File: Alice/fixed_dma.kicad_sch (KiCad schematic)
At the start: 146 parts, among them Q285 NOT_OC, Q286 NOT_OC, Q287 NOT_OC, Q288 NOT_OC, Q289 NOT_OC, Q290 NOT_OC, Q291 NOT_OC, Q292 NOT_OC, Q293 NOT_OC, Q294 NOT_OC, Q295 NOT_OC, Q296 NOT_OC, Q297 NOT_OC, Q298 NOT_OC, Q299 NOT_OC, Q300 NOT_OC, Q301 NOT_OC, Q302 NOT_OC, Q303 NOT_OC, Q304 NOT_OC, Q305 NOT_OC, Q306 NOT_OC, Q307 NOT_OC, Q308 NOT_OC, Q309 NOT_OC, Q310 NOT_OC, Q311 NOT_OC, Q312 NOT_OC, Q313 NOT_OC, Q314 NOT_OC, Q315 NOT_OC, Q316 NOT_OC, Q317 NOT_OC, Q318 NOT_OC, Q319 NOT_OC, Q320 NOT_OC, Q321 NOT_OC, Q322 NOT_OC, Q323 NOT_OC, Q324 NOT_OC, Q325 NOT_OC, Q326 NOT_OC, Q327 NOT_OC, Q328 NOT_OC, Q329 NOT_OC, Q330 NOT_OC, Q331 NOT_OC, Q332 NOT_OC

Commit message: Plane DMA sheet added
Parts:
- added NOR_23, NOR_25: NOR3, symbol NMOS:NOR3
- added NOR_24, NOR_26, NOR_27: NOR2, symbol NMOS:NOR2
- added RRW_FF1, RRW_FF2: DFF, symbol NMOS:DFF
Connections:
- net CCKF: now also RRW_FF2.4 (C1)
- net CCKQF: now also RRW_FF2.5 (C2)
- net DDBR: now also NOR_25.3
- net DKR: now also NOR_23.2
- net PHI1: now also RRW_FF1.4 (C1)
- net PHI2: now also RRW_FF1.5 (C2)
- net VCC: now also NOR_26.3
- new net: NOR_25.1, NOR_27.2
- new net: NOR_25.2, RRW_FF2.1 (Q)
- new net: NOR_24.1, NOR_25.4
- new net: NOR_26.1, NOR_27.3
- new net: RRW_FF1.1 (Q), RRW_FF2.3 (D)
- new net: NOR_23.1, RRW_FF1.3 (D)
- new net C1: NOR_24.2
- new net C3: NOR_24.3
- new net PAD_PRW: NOR_26.2
- new net PAD_RRW: NOR_27.1
- new net UBPD: NOR_23.4
- new net UBQD: NOR_23.3
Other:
- note added: "RE#"
- note added: "Refresh"
- moved on the sheet: RFP_FF1, URP_FF1

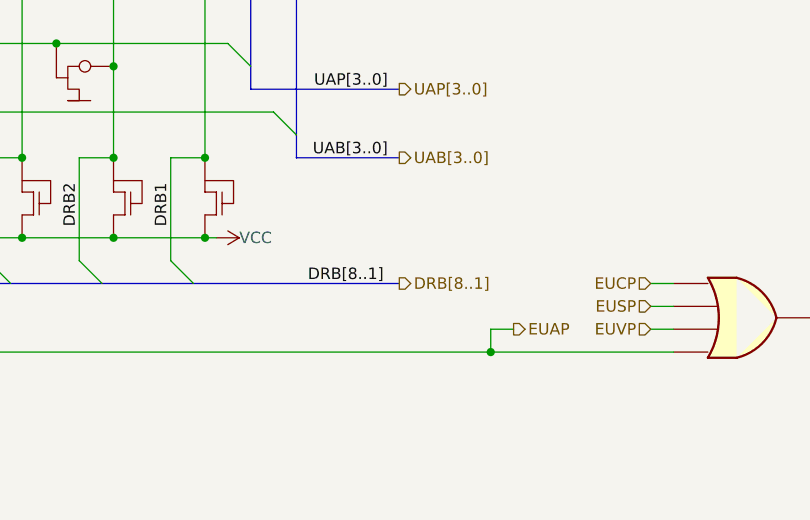
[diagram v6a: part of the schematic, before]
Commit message: Bitplane DMA runs in simulation
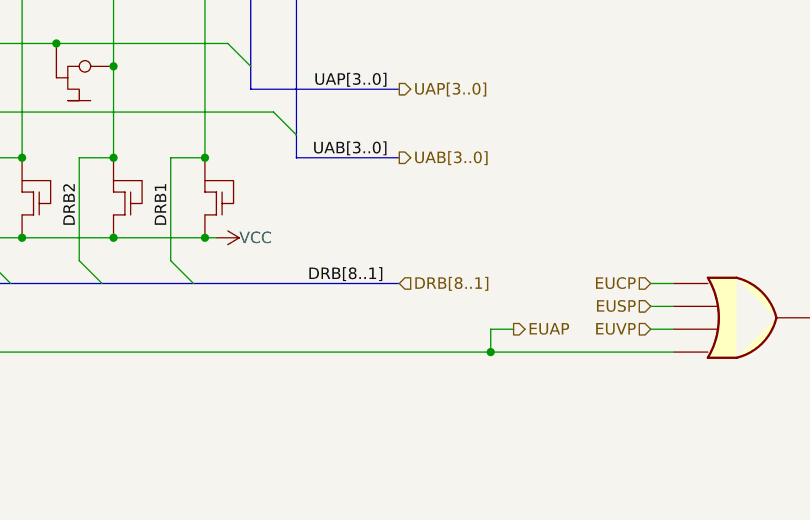
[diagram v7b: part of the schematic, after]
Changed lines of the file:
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@@
     (effects (font (size 1.27 1.27)) (justify left))
   )
-  (hierarchical_label "DRB[8..1]" (shape output) (at 256.54 332.74 0)
+  (hierarchical_label "DRB[8..1]" (shape input) (at 256.54 332.74 0)
     (effects (font (size 1.27 1.27)) (justify left))
   )

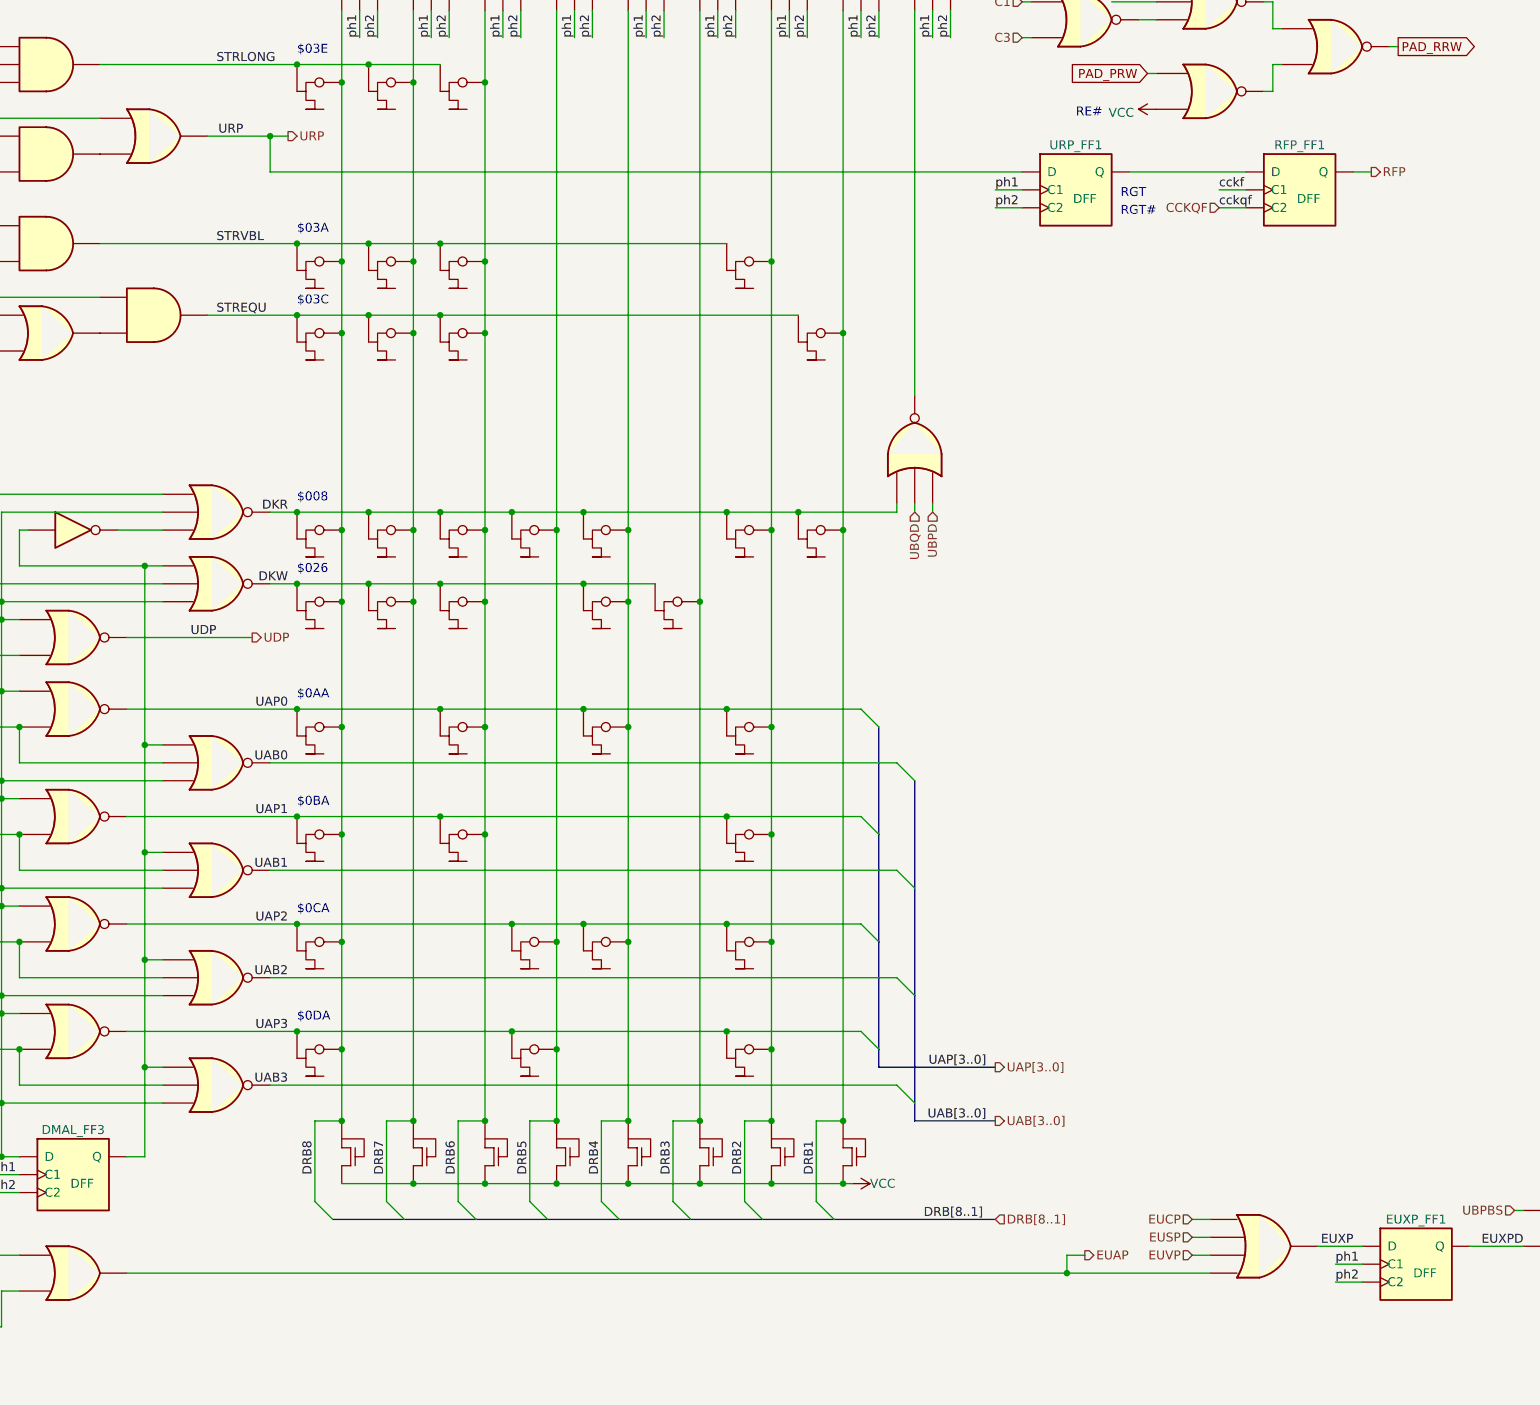
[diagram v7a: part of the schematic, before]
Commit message: Schematics have been annotated
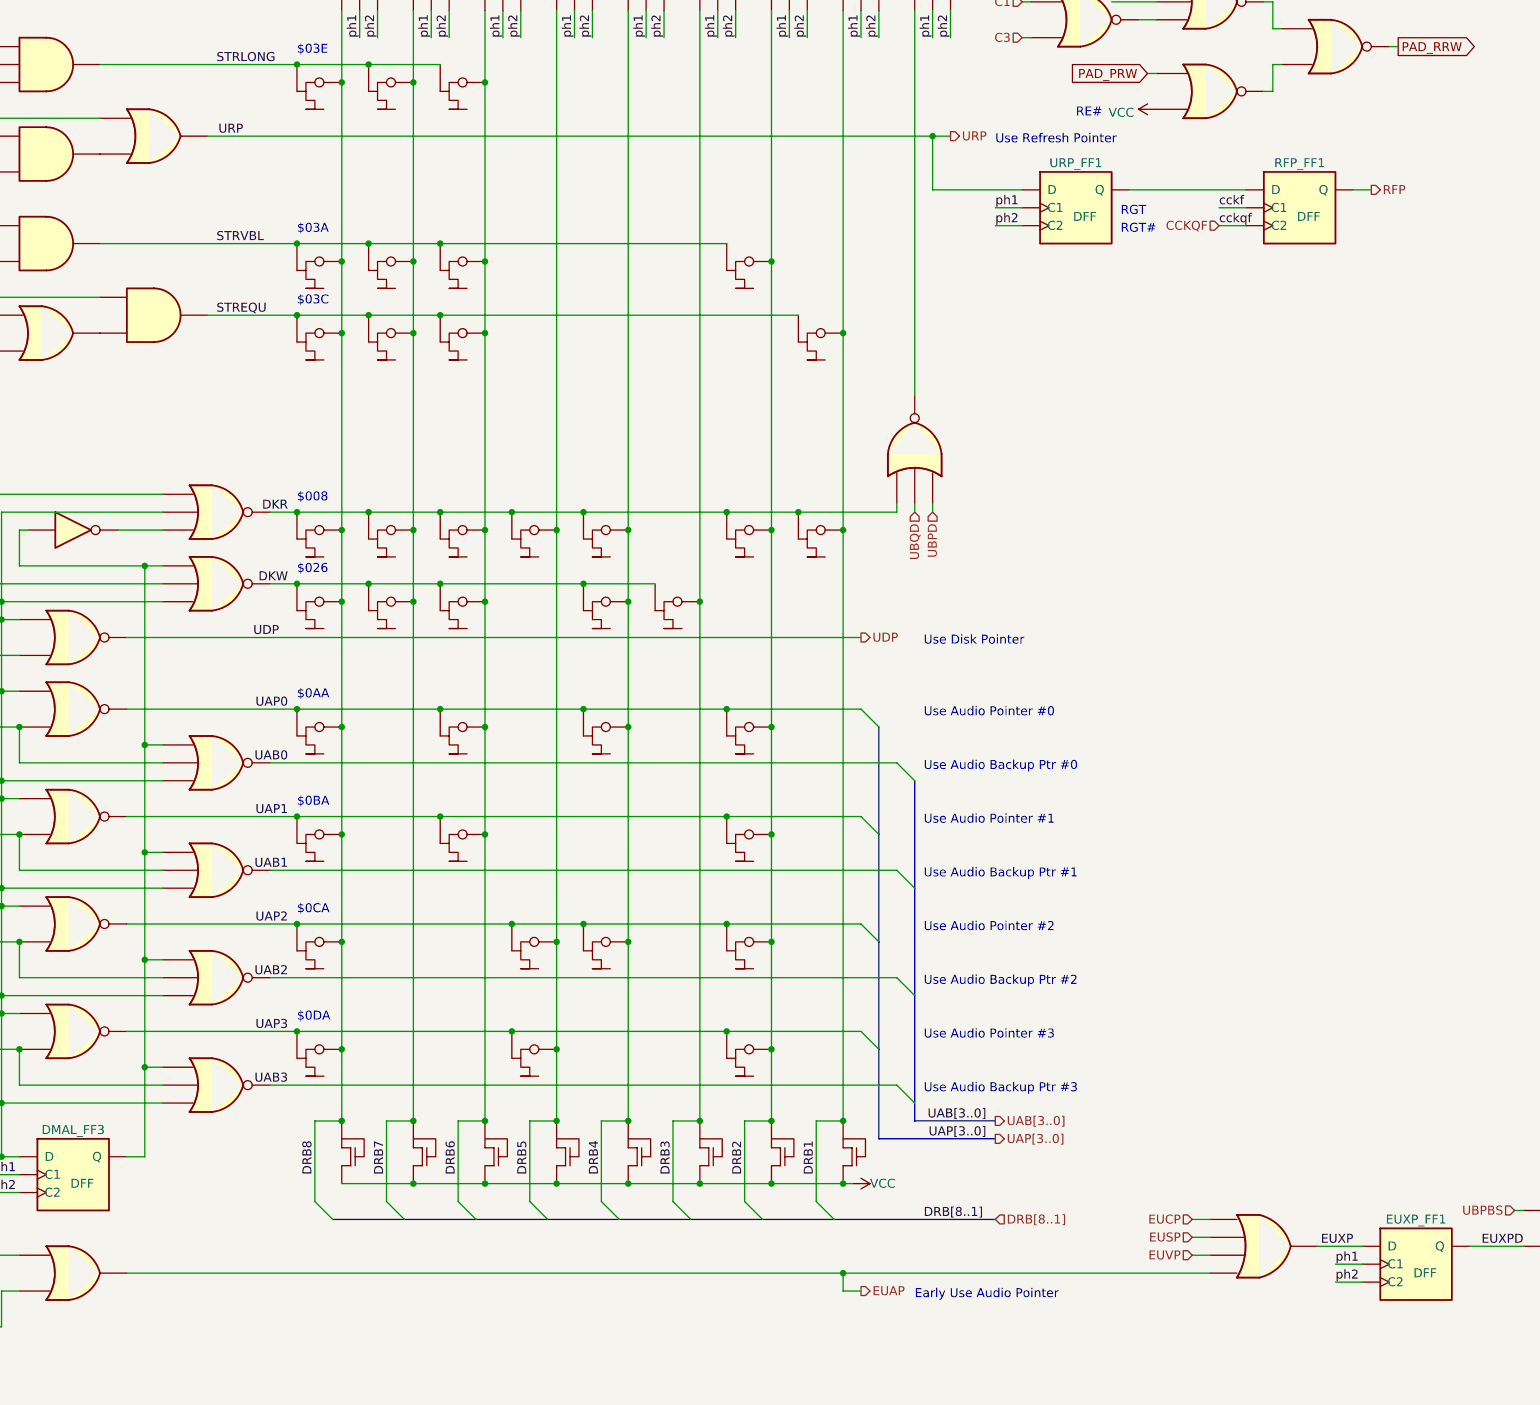
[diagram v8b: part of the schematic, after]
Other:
- note added: "Early Use Audio Pointer"
- note added: "Use Audio Backup Ptr #0"
- note added: "Use Audio Backup Ptr #1"
- note added: "Use Audio Backup Ptr #2"
- note added: "Use Audio Backup Ptr #3"
- note added: "Use Audio Pointer #0"
- note added: "Use Audio Pointer #1"
- note added: "Use Audio Pointer #2"
- note added: "Use Audio Pointer #3"
- note added: "Use Disk Pointer"
- note added: "Use Refresh Pointer"
- moved on the sheet: RFP_FF1, URP_FF1
